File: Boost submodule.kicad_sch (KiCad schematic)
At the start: 2 parts, among them U47 TPS55332QPWPRQ1, U48 TPL0102-100PWR

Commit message: HW-61 chore: FT4233 Wire'd up
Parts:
- removed U47: TPS55332QPWPRQ1, digikey:PWP20_2P45X3P2-L, symbol digikey:TPS55332QPWPRQ1
- removed U48: TPL0102-100PWR, semiconductor:TSSOP-14_P0.65_4.4x5x1.2, symbol integrated-circuit:TPL0102-100PWR
- added C160, C172: 10uF-1210_01, passive:Capacitor_1210, symbol capacitor:10uF-1210_01
- added C161, C165: 100nF-0402_01, passive:Capacitor_0402, symbol capacitor:100nF-0402_01
- added C163: 2.2nF-0402_01, passive:Capacitor_0402, symbol capacitor:2.2nF-0402_01
- added C168: 470nF-0402_01, passive:Capacitor_0402, symbol capacitor:470nF-0402_01
- added C169: 1nF-0402_01, passive:Capacitor_0402, symbol capacitor:1nF-0402_01
- added D2, D4: VS30BQ100HM3, staging:DO-214AB (SMC), symbol staging:VS30BQ100HM3
- added K2, K4: UB2-5NU, electromechanical:UB2-XNX, symbol electromechanical:UB2-5NU
- added L4: 22uH-4747, passive:Inductor_0402, symbol staging:22uH-4747
- added Q1: RUC002N05, semiconductor:SOT23-3-INV_P0.95_2.92x1.3x1.12, symbol semiconductor:RUC002N05
- added Q3, Q5, Q7: FDT439N, staging:SOT223-4_P2.3_3.5x6.5x1.8 -2, symbol staging:FDT439N
- added R115, R117, R118, R134, R140: 10k-0402_02, passive:Resistor_0402, symbol resistor:10k-0402_02
- added R120: 2k-0402_02, passive:Resistor_0402, symbol resistor:2k-0402_02
- added R123: 49.9k-0402, passive:Resistor_0402, symbol staging:49.9k-0402
- added R125: 4.99k-0402, passive:Resistor_0402, symbol staging:4.99k-0402
- added R127: 0R-0402_01, passive:Resistor_0402, symbol resistor:0R-0402_01
- added R128: 150k-0402_02, passive:Resistor_0402, symbol staging:150k-0402_02
- added R131: 1k-0402_02, passive:Resistor_0402, symbol resistor:1k-0402_02
- added R133: 267k-0402_01, passive:Resistor_0402, symbol resistor:267k-0402_01
- added U59, U61: LTC4359CDCB#TRMPBF, 05-08-1715_ADI, symbol staging:LTC4359CDCB-TRMPBF
- added U62: TPS55332QPWPRQ1, digikey:HTSOP-20_P1.63_6.5x4.4mm, symbol staging:TPS55332QPWPRQ1
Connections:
- net EN: now also R140.1, U62.5 (EN)
- new net: C168.1, U62.11 (SS)
- new net: C163.1, U62.9 (Cdly)
- new net: R125.2, U62.7 (Rslew)
- new net: C165.1, U62.20 (BOOT)
- new net: R133.1, R134.2, U62.13 (RST_TH)
- new net: D2.1 (Anode), L4.1, R127.2
- new net: D4.1 (Anode), L4.2, U62.18 (SW)
- new net: Q1.2 (G), R115.2
- new net: C161.2, R128.1, R131.2, U62.14 (VSENSE)
- new net: Q3.1 (G), Q5.1 (G), U59.2 (GATE)
- new net: Q3.2 (S), Q5.2 (S), U59.3 (SOURCE)
- new net: R123.2, U62.6 (RT)
- new net: R120.1, U62.8 (~{RST})
- new net: C161.1, U62.15 (COMP)
- new net: Q7.1 (G), U61.2 (GATE)
- new net +24V: Q7.3 (D), U61.4 (IN)
- new net +5V: Q3.3 (D), R118.2, U59.4 (IN)
- new net 24V_ENABLE: R117.1, U61.5 (~{SHDN})
- new net 5V_ENABLE: Q1.3 (D), R118.1, U59.5 (~{SHDN})
- new net BOOST_OUT_REF_V: C169.1, C172.1, D4.2 (N/C), R120.2, R128.2, R133.2, U62.16 (VReg)
- new net BOOST_PS: C160.1, D2.2 (N/C), Q5.3 (D), Q7.2 (S), R127.1, U59.1 (OUT), U61.1 (OUT), U61.3 (SOURCE), U62.19 (VIN)
- new net DIGIPOT_IN: R131.1
- new net EN_24V_BOOST_SOURCE: R115.1, R117.2
- new net GND: C160.2, C163.2, C165.2, C168.2, C169.2, C172.2, Q1.1 (S), R123.1, R125.1, R134.1, R140.2, U59.6 (VSS), U59.7 (VSS), U61.6 (VSS), U61.7 (VSS), U62.10 (GND), U62.12 (GND), U62.17 (PGND), U62.21 (EPAD), U62.3 (SYNC), U62.4 (GND)
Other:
- added sheet Current shunt (current_sensing.kicad_sch)
- note added: "Find better relays as plan B for boost power source switch"
- note added: "Output V over digiPot Resistance y = Vout (V) x = digipot Resistance (kOhm)"
- note added: "SET EN LOW during boost input switchin so the TPS doesn't turn off Due to Low voltage output protection."
- note added: "This diode is recomended but didn't worked in simulation short it if needed"

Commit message: Details to finish
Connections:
- net EN_24V_BOOST_SOURCE: no longer R115.1
- net EN renamed EN_BOOST
- new net EN_5V_BOOST_SOURCE: R115.1
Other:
- moved on the sheet: C160, C161, C163, C165, C168, C169, C172, D2, D4, K2, K4, L4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

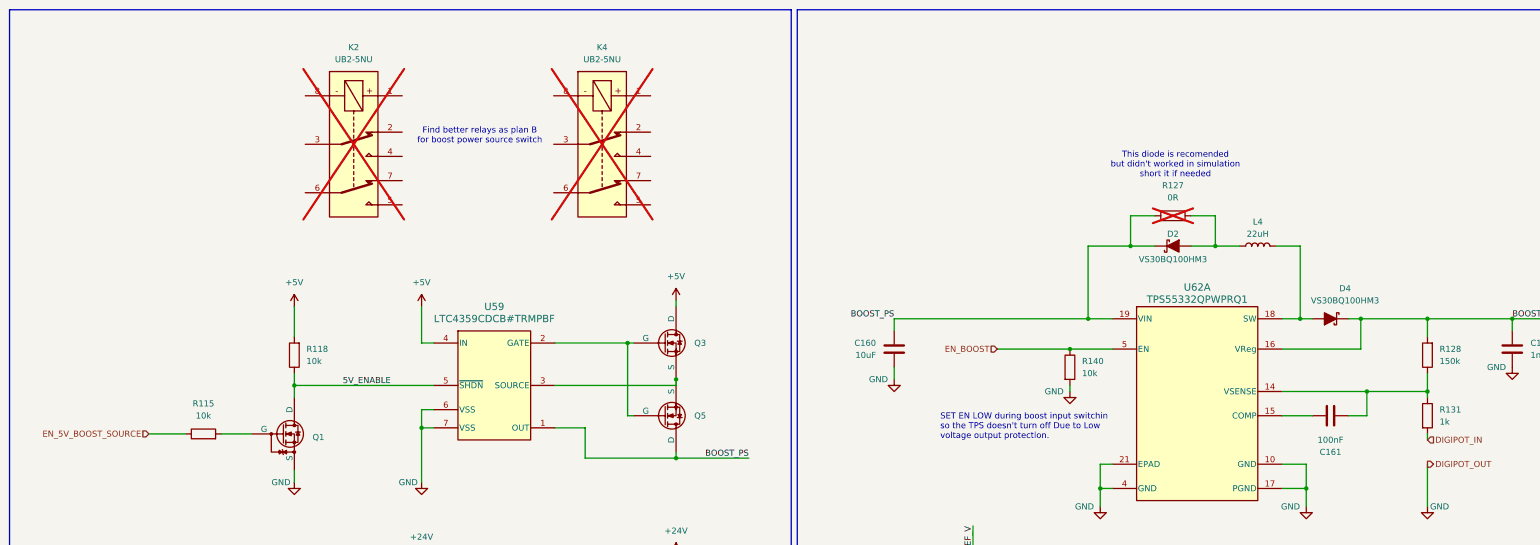
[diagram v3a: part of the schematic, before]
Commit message: HW-61/chore: Added simulation for switch ocntrol, organized the overall schematic, fixed the ERC errors. Still pending for the current sense components and negative side LDO control
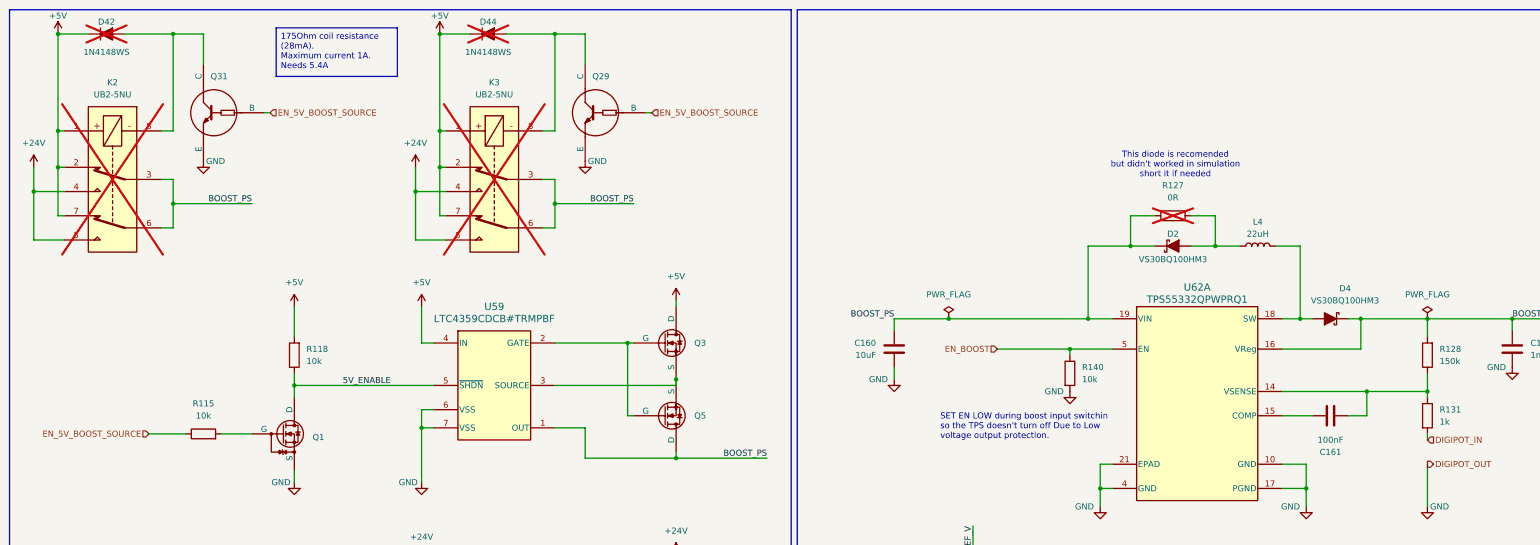
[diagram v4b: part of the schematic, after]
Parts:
- removed K4: UB2-5NU, electromechanical:UB2-XNX, symbol electromechanical:UB2-5NU
- added D42, D44: 1N4148WS, semiconductor:SOD323FL_P2.25_1.7x1.25x0.9, symbol semiconductor:1N4148WS
- added K3: UB2-5NU, electromechanical:UB2-XNX, symbol electromechanical:UB2-5NU
- added Q29, Q31: DTC143TET1G, semiconductor:SC-75-3_P0.5_1.6x0.8x0.8, symbol semiconductor:DTC143TET1G
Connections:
- net +24V: now also K2.4, K2.5, K3.4, K3.5
- net +5V: now also K2.1, K2.2, K2.7, D42.1 (Cathode), D44.1 (Cathode), K3.1, K3.2, K3.7
- net BOOST_PS: now also K2.3, K2.6, K3.3, K3.6
- net EN_5V_BOOST_SOURCE: now also Q29.1 (B), Q31.1 (B)
- net GND: now also Q29.2 (E), Q31.2 (E)
- net at K2.8: now also D42.2 (Anode), Q31.3 (C)
- new net: D44.2 (Anode), K3.8, Q29.3 (C)
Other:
- note removed: "Find better relays as plan B for boost power source switch"
- moved on the sheet: K2, R140
